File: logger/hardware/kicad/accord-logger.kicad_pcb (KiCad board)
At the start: 2 copper layers, 120 x 80 mm, 117 parts, among them J1 Board connector 14-way, J3 Spare GP13 / switched power, J4 Reset RUN-GND, J5 SD breakout 6-way, Q1 MMBT3904, Q2 BSS138P, Q3 BSS138P, Q4 BSS138P, Q5 IPD50P04P4L-11, Q6 2N3904, Q7 2N3904, U1 RaspberryPi_Pico_W, U15 MAX3485, U16 DS3231SN, U2 PC817, U3 ASSR-601JV, U4 TPS70950QDBVRQ1, U5 TPS3839K50DBZR, U6 LM2678T-5.0

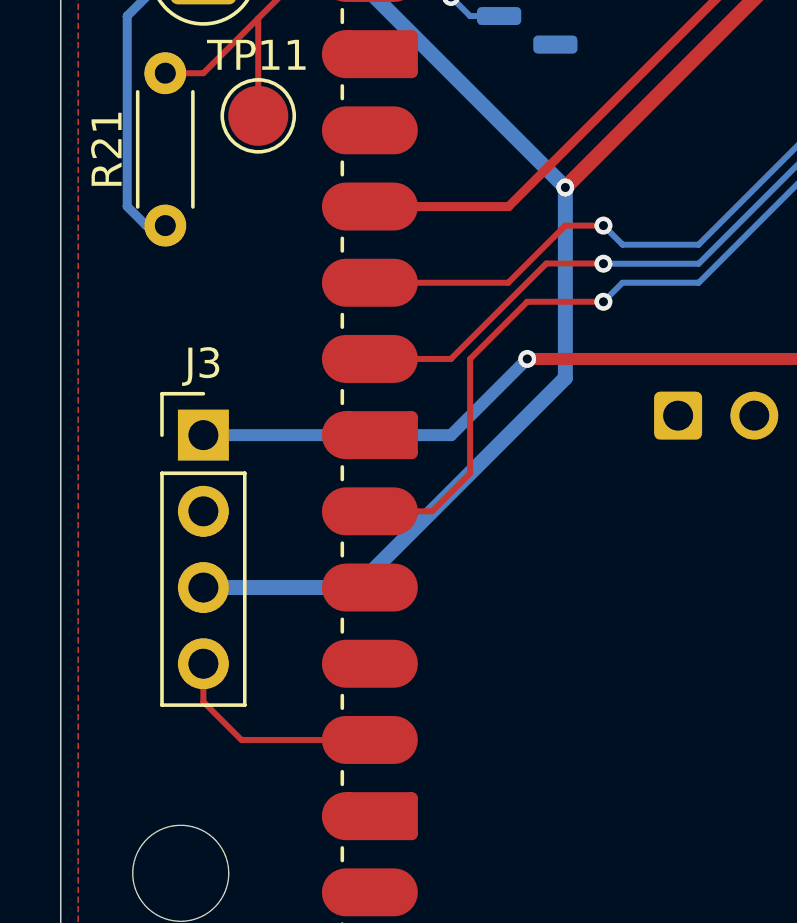
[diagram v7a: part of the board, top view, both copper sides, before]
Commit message: layout: J3 2x03 placed and routed
Owner updated the board from the schematic (J3 1x04 -> 2x03,
D-HDR-16) and placed J3 at (92.07, 121.28) by Pico pins 15-17, clear of
H4 and R21. B5, switched 3V3, GP11, GP12 and GP13 routed; pins 3 and 4
routed GP13 / 3V3, which the next commit adopts in the schematic. The
.kicad_pro change is KiCad's default pad size from the owner's session.

Refilled scratch DRC: no errors beyond the Pico footprint's own paste
items, unconnected only Q5's middle lead.

Claude-Session-ID: d2c32eb9-406b-48d8-b5b5-bb1d8d4746af
Co-Authored-By: Claude Opus 5.5 <noreply@anthropic.com>
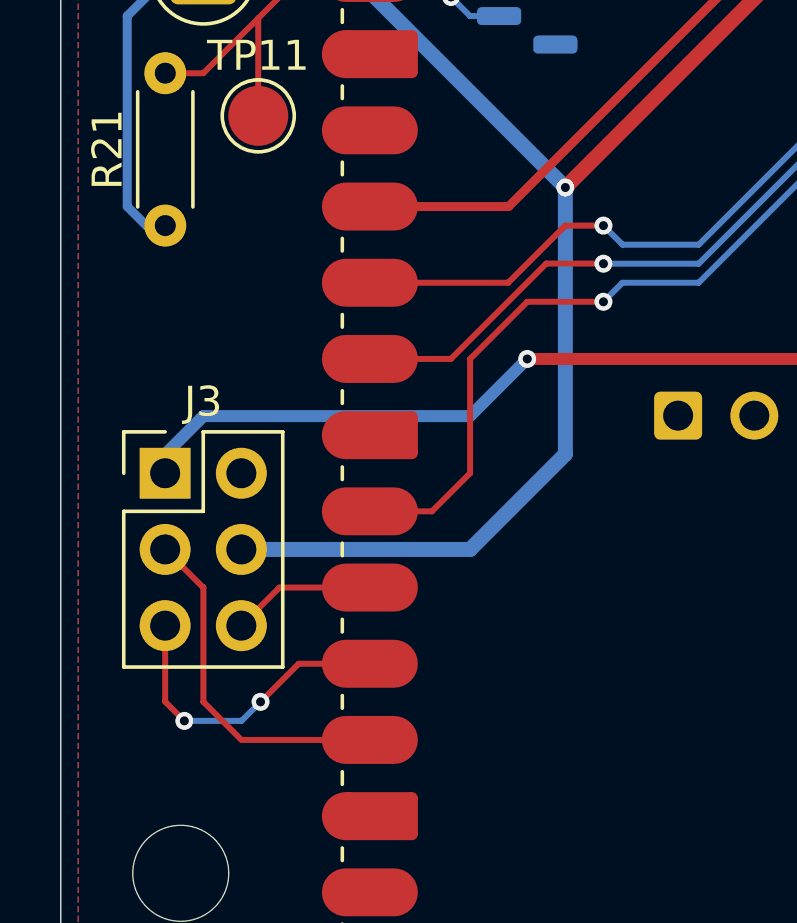
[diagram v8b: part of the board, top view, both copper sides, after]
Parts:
- J3: value Spare GP13 / switched power -> Spare GP11-13 / switched power; footprint Connector_PinHeader_2.54mm:PinHeader_1x04_P2.54mm_Vertical -> Connector_PinHeader_2.54mm:PinHeader_2x03_P2.54mm_Vertical
- moved J3 1.80 mm to (92.1, 121.3)
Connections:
- J3 pad 3: /P3V3_SW -> /SPARE_GP13
- J3 pad 4: /SPARE_GP13 -> /P3V3_SW
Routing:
- net /SPARE_GP12: track 0.00 -> 10.4 mm, vias 0 -> 2
- net /SPARE_GP11: track 0.00 -> 4.81 mm
- net /SPARE_GP13: track 7.35 -> 11.7 mm
- net /B5: track 134.1 -> 136.2 mm
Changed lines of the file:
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@@
 		)
 	)
-	(footprint "Connector_PinHeader_2.54mm:PinHeader_1x04_P2.54mm_Vertical"
+	(footprint "Connector_PinHeader_2.54mm:PinHeader_2x03_P2.54mm_Vertical"
 		(layer "F.Cu")
-		(at 93.345 120.015)
-		(descr "Through hole straight pin header, 1x04, 2.54mm pitch, single row")
-		(tags "Through hole pin header THT 1x04 2.54mm single row")
+		(at 92.07 121.285)
+		(descr "Through hole straight pin header, 2x03, 2.54mm pitch, double rows")
+		(tags "Through hole pin header THT 2x03 2.54mm double row")
 		(property "Reference" "J3"
-			(at 0 -2.38 0)
+			(at 1.27 -2.38 0)
 			(layer "F.SilkS")
 			(effects
@@
 			)
 		)
-		(property "Value" "Spare GP13 / switched power"
-			(at 0 10 0)
+		(property "Value" "Spare GP11-13 / switched power"
+			(at 1.27 7.46 0)
 			(layer "F.Fab")
 			(effects
@@
 			)
 		)
-		(property ki_fp_filters "Connector*:*_1x??_*")
+		(property ki_fp_filters "Connector*:*_2x??_*")
 		(sheetname "/")
 		(sheetfile "accord-logger.kicad_sch")
@@
 		(fp_line
 			(start -1.38 1.27)
-			(end -1.38 9)
+			(end -1.38 6.46)
 			(stroke
 				(width 0.12)
@@
 		(fp_line
 			(start -1.38 1.27)
-			(end 1.38 1.27)
+			(end 1.27 1.27)
 			(stroke
 				(width 0.12)
@@
 		)
 		(fp_line
-			(start -1.38 9)
-			(end 1.38 9)
+			(start -1.38 6.46)
+			(end 3.92 6.46)
 			(stroke
 				(width 0.12)
@@
 		)
 		(fp_line
-			(start 1.38 1.27)
-			(end 1.38 9)
+			(start 1.27 -1.38)
+			(end 3.92 -1.38)
+			(stroke
+				(width 0.12)
+				(type solid)
+			)
+			(layer "F.SilkS")
+		)
+		(fp_line
+			(start 1.27 1.27)
+			(end 1.27 -1.38)
+			(stroke
+				(width 0.12)
+				(type solid)
+			)
+			(layer "F.SilkS")
+		)
+		(fp_line
+			(start 3.92 -1.38)
+			(end 3.92 6.46)
 			(stroke
 				(width 0.12)
@@
 		(fp_line
 			(start -1.77 -1.77)
-			(end -1.77 9.39)
+			(end -1.77 6.85)
 			(stroke
 				(width 0.05)
@@
 		)
 		(fp_line
-			(start -1.77 9.39)
-			(end 1.77 9.39)
+			(start -1.77 6.85)
+			(end 4.32 6.85)
 			(stroke
 				(width 0.05)
@@
 		)
 		(fp_line
-			(start 1.77 -1.77)
+			(start 4.32 -1.77)
 			(end -1.77 -1.77)
 			(stroke
@@
 		)
 		(fp_line
-			(start 1.77 9.39)
-			(end 1.77 -1.77)
+			(start 4.32 6.85)
+			(end 4.32 -1.77)
 			(stroke
 				(width 0.05)
@@
 		)
 		(fp_line
-			(start -1.27 -0.635)
-			(end -0.635 -1.27)
+			(start -1.27 0)
+			(end 0 -1.27)
 			(stroke
 				(width 0.1)
@@
 		)
 		(fp_line
-			(start -1.27 8.89)
-			(end -1.27 -0.635)
+			(start -1.27 6.35)
+			(end -1.27 0)
 			(stroke
 				(width 0.1)
@@
 		)
 		(fp_line
-			(start -0.635 -1.27)
-			(end 1.27 -1.27)
+			(start 0 -1.27)
+			(end 3.81 -1.27)
 			(stroke
 				(width 0.1)
@@
 		)
 		(fp_line
-			(start 1.27 -1.27)
-			(end 1.27 8.89)
+			(start 3.81 -1.27)
+			(end 3.81 6.35)
 			(stroke
 				(width 0.1)
@@
 		)
 		(fp_line
-			(start 1.27 8.89)
-			(end -1.27 8.89)
+			(start 3.81 6.35)
+			(end -1.27 6.35)
 			(stroke
 				(width 0.1)
@@
 		)
 		(fp_text user "${REFERENCE}"
-			(at 0 3.81 90)
+			(at 1.27 2.54 90)
 			(layer "F.Fab")
 			(effects
@@
 		)
 		(pad "2" thru_hole circle
-			(at 0 2.54)
+			(at 2.54 0)
 			(size 1.7 1.7)
 			(drill 1)
@@
 		)
 		(pad "3" thru_hole circle
-			(at 0 5.08)
+			(at 0 2.54)
 			(size 1.7 1.7)
 			(drill 1)
 			(layers "*.Cu" "*.Mask")
 			(remove_unused_layers no)
-			(net 5 "/P3V3_SW")
+			(net 28 "/SPARE_GP13")
 			(pinfunction "Pin_3")
 			(pintype "passive")
 		)
 		(pad "4" thru_hole circle
-			(at 0 7.62)
+			(at 2.54 2.54)
 			(size 1.7 1.7)
 			(drill 1)
 			(layers "*.Cu" "*.Mask")
 			(remove_unused_layers no)
-			(net 28 "/SPARE_GP13")
+			(net 5 "/P3V3_SW")
 			(pinfunction "Pin_4")
 			(pintype "passive")
 		)
+		(pad "5" thru_hole circle
+			(at 0 5.08)
+			(size 1.7 1.7)
+			(drill 1)
+			(layers "*.Cu" "*.Mask")
+			(remove_unused_layers no)
+			(net 43 "/SPARE_GP12")
+			(pinfunction "Pin_5")
+			(pintype "passive")
+		)
+		(pad "6" thru_hole circle
+			(at 2.54 5.08)
+			(size 1.7 1.7)
+			(drill 1)
+			(layers "*.Cu" "*.Mask")
+			(remove_unused_layers no)
+			(net 42 "/SPARE_GP11")
+			(pinfunction "Pin_6")
+			(pintype "passive")
+		)
 		(embedded_fonts no)
-		(model "${KICAD9_3DMODEL_DIR}/Connector_PinHeader_2.54mm.3dshapes/PinHeader_1x04_P2.54mm_Vertical.step"
+		(model "${KICAD9_3DMODEL_DIR}/Connector_PinHeader_2.54mm.3dshapes/PinHeader_2x03_P2.54mm_Vertical.step"
 			(offset
 				(xyz 0 0 0)
@@
 	)
 	(segment
-		(start 98.425 125.095)
-		(end 93.345 125.095)
-		(width 0.5)
-		(layer "B.Cu")
-		(net 5)
-	)
-	(segment
 		(start 93.345 104.557183)
 		(end 98.207183 104.557183)
@@
 	)
 	(segment
+		(start 105.41 111.76)
+		(end 105.41 120.65)
+		(width 0.5)
+		(layer "B.Cu")
+		(net 5)
+	)
+	(segment
 		(start 146.467183 114.935)
 		(end 139.3825 114.935)
@@
 	)
 	(segment
+		(start 102.235 123.825)
+		(end 94.61 123.825)
+		(width 0.5)
+		(layer "B.Cu")
+		(net 5)
+	)
+	(segment
 		(start 124.46 97.155)
 		(end 124.46 86.36)
@@
 	)
 	(segment
-		(start 105.41 118.11)
-		(end 98.425 125.095)
-		(width 0.5)
-		(layer "B.Cu")
-		(net 5)
-	)
-	(segment
 		(start 92.075 113.03)
 		(end 91.44 113.03)
@@
 	)
 	(segment
-		(start 105.41 111.76)
-		(end 105.41 118.11)
+		(start 105.41 120.65)
+		(end 102.235 123.825)
 		(width 0.5)
 		(layer "B.Cu")
@@
 	)
 	(segment
+		(start 93.345 119.38)
+		(end 92.07 120.655)
+		(width 0.4)
+		(layer "B.Cu")
+		(net 10)
+	)
+	(segment
 		(start 174.63 123.694823)
 		(end 177.674823 120.65)
@@
 	)
 	(segment
+		(start 104.14 117.475)
+		(end 102.235 119.38)
+		(width 0.4)
+		(layer "B.Cu")
+		(net 10)
+	)
+	(segment
 		(start 172.09 123.835)
 		(end 174.489823 123.835)
@@
 	)
 	(segment
+		(start 102.235 119.38)
+		(end 93.345 119.38)
+		(width 0.4)
+		(layer "B.Cu")
+		(net 10)
+	)
+	(segment
 		(start 142.24 120.015)
 		(end 140.97 121.285)
@@
 	)
 	(segment
-		(start 93.345 120.015)
-		(end 101.6 120.015)
+		(start 174.489823 123.835)
+		(end 174.63 123.694823)
 		(width 0.4)
 		(layer "B.Cu")
@@
 	)
 	(segment
-		(start 174.489823 123.835)
-		(end 174.63 123.694823)
+		(start 140.97 121.285)
+		(end 127.635 121.285)
 		(width 0.4)
 		(layer "B.Cu")
@@
 	)
 	(segment
-		(start 140.97 121.285)
-		(end 127.635 121.285)
+		(start 92.07 120.655)
+		(end 92.07 121.285)
 		(width 0.4)
 		(layer "B.Cu")
@@
 	)
 	(segment
-		(start 101.6 120.015)
-		(end 104.14 117.475)
-		(width 0.4)
-		(layer "B.Cu")
-		(net 10)
-	)
-	(segment
 		(start 98.895 97.155)
 		(end 102.235 97.155)
@@
 	)
 	(segment
+		(start 94.615 130.175)
+		(end 93.345 128.905)
+		(width 0.2)
+		(layer "F.Cu")
+		(net 28)
+	)
+	(segment
+		(start 93.345 125.09)
+		(end 93.335 125.09)
+		(width 0.2)
+		(layer "F.Cu")
+		(net 28)
+	)
+	(segment
 		(start 93.345 128.905)
-		(end 94.615 130.175)
+		(end 93.345 125.09)
 		(width 0.2)
 		(layer "F.Cu")
@@
 	)
 	(segment
-		(start 94.615 130.175)
-		(end 98.895 130.175)
+		(start 98.895 130.175)
+		(end 94.615 130.175)
 		(width 0.2)
 		(layer "F.Cu")
@@
 	)
 	(segment
-		(start 93.345 127.635)
-		(end 93.345 128.905)
+		(start 93.335 125.09)
+		(end 92.07 123.825)
 		(width 0.2)
 		(layer "F.Cu")
@@
 	)
 	(segment
+		(start 98.895 125.095)
+		(end 95.88 125.095)
+		(width 0.2)
+		(layer "F.Cu")
+		(net 42)
+	)
+	(segment
+		(start 95.88 125.095)
+		(end 94.61 126.365)
+		(width 0.2)
+		(layer "F.Cu")
+		(net 42)
+	)
+	(segment
+		(start 92.71 129.54)
+		(end 92.07 128.9)
+		(width 0.2)
+		(layer "F.Cu")
+		(net 43)
+	)
+	(segment
+		(start 98.895 127.635)
+		(end 96.52 127.635)
+		(width 0.2)
+		(layer "F.Cu")
+		(net 43)
+	)
+	(segment
+		(start 96.52 127.635)
+		(end 95.25 128.905)
+		(width 0.2)
+		(layer "F.Cu")
+		(net 43)
+	)
+	(segment
+		(start 92.07 128.9)
+		(end 92.07 126.365)
+		(width 0.2)
+		(layer "F.Cu")
+		(net 43)
+	)
+	(via
+		(at 95.25 128.905)
+		(size 0.6)
+		(drill 0.3)
+		(layers "F.Cu" "B.Cu")
+		(net 43)
+	)
+	(via
+		(at 92.71 129.54)
+		(size 0.6)
+		(drill 0.3)
+		(layers "F.Cu" "B.Cu")
+		(net 43)
+	)
+	(segment
+		(start 94.615 129.54)
+		(end 92.71 129.54)
+		(width 0.2)
+		(layer "B.Cu")
+		(net 43)
+	)
+	(segment
+		(start 95.25 128.905)
+		(end 94.615 129.54)
+		(width 0.2)
+		(layer "B.Cu")
+		(net 43)
+	)
+	(segment
